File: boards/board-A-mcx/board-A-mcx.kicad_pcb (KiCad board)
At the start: 4 copper layers, 76.3 x 138.5 mm, 30 parts, among them J5 SAMTEC_QSE-040-01-X-D-A, K0 Samtec_MCX-J-P-X-ST-SM1, K1 Samtec_MCX-J-P-X-ST-SM1, K10 Samtec_MCX-J-P-X-ST-SM1, K11 Samtec_MCX-J-P-X-ST-SM1, K12 Samtec_MCX-J-P-X-ST-SM1, K13 Samtec_MCX-J-P-X-ST-SM1, K14 Samtec_MCX-J-P-X-ST-SM1, K15 Samtec_MCX-J-P-X-ST-SM1, K16 Samtec_MCX-J-P-X-ST-SM1, K17 Samtec_MCX-J-P-X-ST-SM1, K18 Samtec_MCX-J-P-X-ST-SM1, K19 Samtec_MCX-J-P-X-ST-SM1, K2 Samtec_MCX-J-P-X-ST-SM1, K20 Samtec_MCX-J-P-X-ST-SM1, K21 Samtec_MCX-J-P-X-ST-SM1, K22 Samtec_MCX-J-P-X-ST-SM1, K23 Samtec_MCX-J-P-X-ST-SM1, K3 Samtec_MCX-J-P-X-ST-SM1, K4 Samtec_MCX-J-P-X-ST-SM1, K5 Samtec_MCX-J-P-X-ST-SM1, K6 Samtec_MCX-J-P-X-ST-SM1, K7 Samtec_MCX-J-P-X-ST-SM1, K8 Samtec_MCX-J-P-X-ST-SM1, K9 Samtec_MCX-J-P-X-ST-SM1

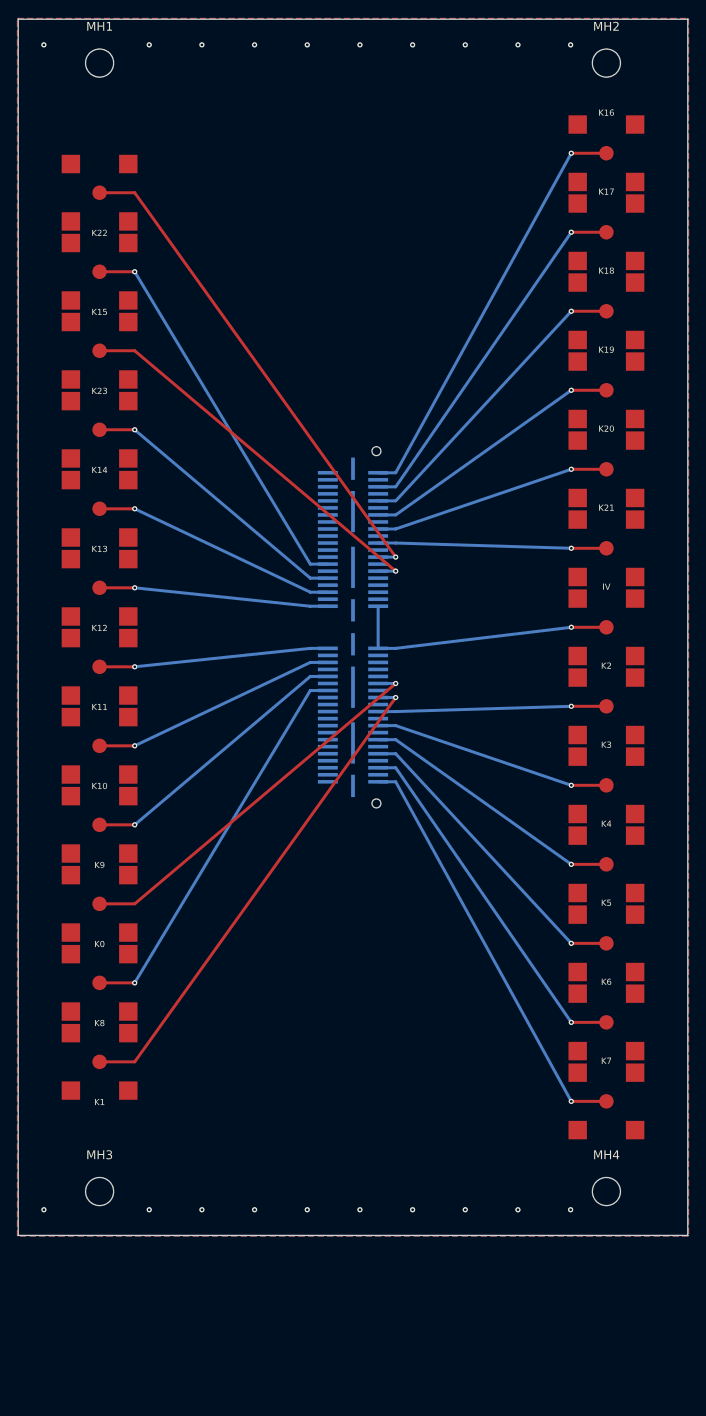
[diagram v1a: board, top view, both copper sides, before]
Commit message: Board A: through-hole MCX + 8/16 planar FreeRouting autoroute (JLC)
Re-lay-out Board A to eliminate the connector-crossing tracks and the
per-jack signal vias the reviewer flagged:

- Jack SMD -> THROUGH-HOLE: Samtec MCX-J-P-H-ST-TH1 (DK SAM8944-ND). The
  plated signal pin reaches every layer, so the QSE B.Cu escape lands on
  it with no face-change via. New datasheet-verified footprint + drawing.
- Placement 12/12 -> 8/16 planar: each jack sits on the edge matching its
  QSE pin column (west 8 = K8-K15, east 16 + IV), a monotonic single-layer
  fan. The old 12/12 forced 4 channels across the connector (the crossings);
  12/12 kept as gen_board SPLIT="balanced" flag.
- Routing now via FreeRouting (KiCad -> .dsn -> autoroute -> .ses), B.Cu
  only: ZERO signal vias, ZERO crossings, all 25 nets on one layer. New
  tools export_dsn.py / import_ses.py / tie_islands.py; finalize_board.py
  gains setup/stitch modes (B/C/D keep the deterministic router).
- Fab JLCPCB-only: 0.325 mm 50 ohm microstrip on JLC04161H-7628 (was 0.34
  on the PCBWay stack); order controlled impedance. Board now 75 x 157 mm.
- DRC 0 violations / 0 unconnected; netlist verified identical to pinout.py.
- Fab package, JLC upload zip, DigiKey BOM, all docs + reference schematic
  regenerated. Purchase total ~$950 (MCX 120 @ $4.21 + QSE 5 + IV adapter 4).

Adversarially verified: board (0 signal vias, single-layer, DRC), fab
package, and cross-doc consistency.

Co-Authored-By: Claude Fable 5 <noreply@anthropic.com>
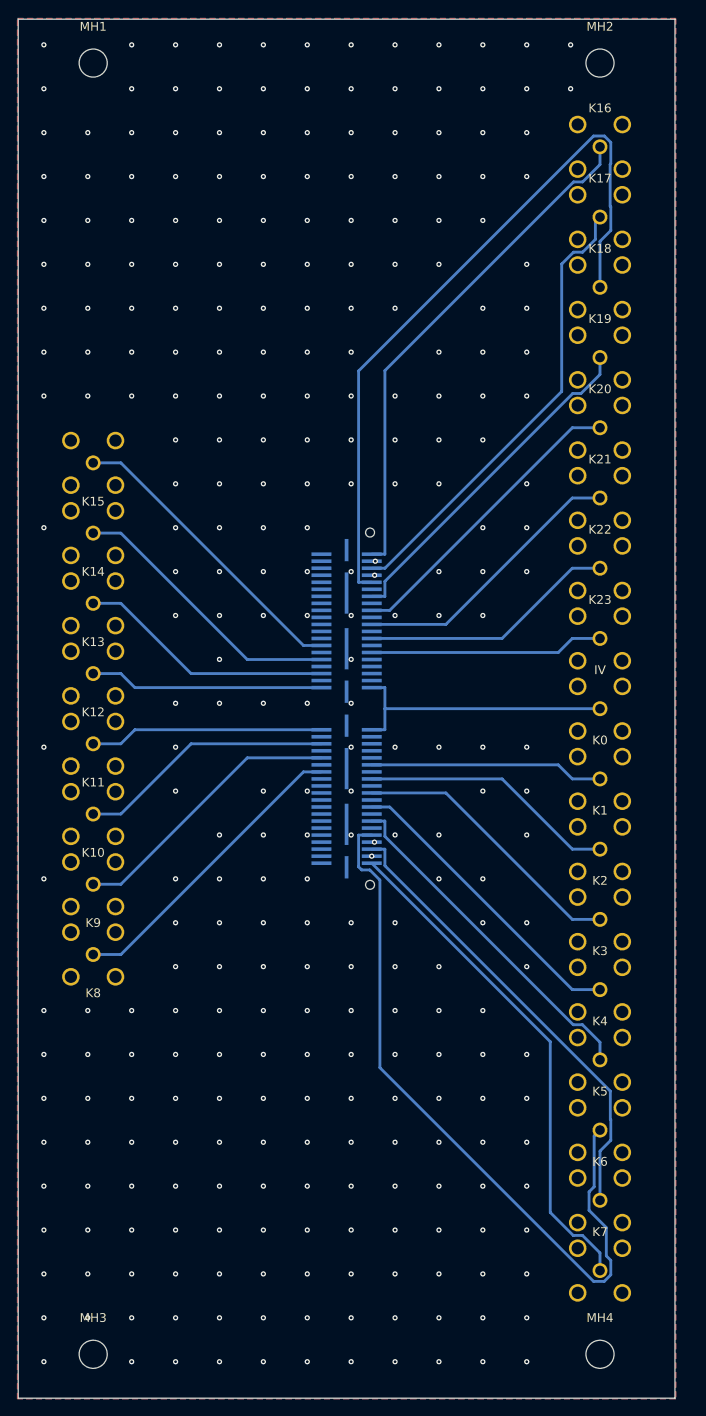
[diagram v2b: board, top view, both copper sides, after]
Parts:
- removed the IV at (76.0, 79.3)
- added IV: Samtec_MCX-J-P-H-ST-TH1, Samtec_MCX-J-P-H-ST-TH1, F.Cu at (75.3, 88.5)
- K0, K1, K10, K11, K12, K13, K14, K15, K16, K17, K18, K19, K2, K20, K21, K22, K23, K3, K4, K5, K6, K7, K8, K9: value Samtec_MCX-J-P-X-ST-SM1 -> Samtec_MCX-J-P-H-ST-TH1; footprint Samtec_MCX-J-P-X-ST-SM1 -> Samtec_MCX-J-P-H-ST-TH1
- moved K22 71.3 mm to (75.3, 72.5), turned to 0 degrees
- moved K23 65.7 mm to (75.3, 80.5), turned to 0 degrees
- moved K1 61.9 mm to (75.3, 104.5), turned to 0 degrees
- moved K0 58.7 mm to (75.3, 96.5), turned to 0 degrees
- moved K2 24.3 mm to (75.3, 112.5)
- moved K3 23.3 mm to (75.3, 120.5)
- moved K4 22.3 mm to (75.3, 128.5)
- moved K15 21.8 mm to (17.5, 60.5)
- moved K5 21.3 mm to (75.3, 136.5)
- moved K6 20.3 mm to (75.3, 144.5)
- moved K7 19.3 mm to (75.3, 152.5)
- moved MH3 18.6 mm to (17.5, 162.1)
- moved MH4 18.6 mm to (75.3, 162.1)
- moved K14 11.8 mm to (17.5, 68.5)
- moved K13 10.8 mm to (17.5, 76.5)
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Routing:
- net SIPM_K5: track 35.4 -> 84.3 mm, vias 1 -> 0
- net SIPM_K18: track 35.4 -> 82.8 mm, vias 1 -> 0
- net SIPM_K1: track 57.1 -> 29.3 mm, vias 1 -> 0
- net SIPM_K22: track 57.1 -> 29.3 mm, vias 1 -> 0
- net SIPM_K23: track 44.9 -> 26.7 mm, vias 1 -> 0
- net SIPM_K0: track 44.9 -> 26.7 mm, vias 1 -> 0
- net SIPM_K6: track 41.2 -> 52.7 mm, vias 1 -> 0
- net SIPM_K16: track 47.5 -> 58.7 mm, vias 1 -> 0
- net SIPM_K17: track 41.2 -> 52.3 mm, vias 1 -> 0
- net SIPM_K7: track 47.5 -> 57.8 mm, vias 1 -> 0
- net SIPM_K15: track 44.8 -> 34.6 mm, vias 1 -> 0
- net SIPM_K8: track 44.8 -> 34.6 mm, vias 1 -> 0
- net SIPM_K4: track 30.5 -> 39.5 mm, vias 1 -> 0
- net SIPM_K19: track 30.5 -> 39.4 mm, vias 1 -> 0
- net SIPM_K3: track 27.1 -> 34.6 mm, vias 1 -> 0
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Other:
- board size 76.3 x 138.5 mm -> 74.8 x 157.1 mm
